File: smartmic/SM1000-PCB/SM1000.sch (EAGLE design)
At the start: 140 parts, among them CN1 HDR100-6, CN2 MOLEX-MINI-B-SMT, CN3 RASM712PX, CN4 RJ-45, CN5 MJ-3523-SMT, CN6 MJ-3523-SMT, CN7 MJ-3523-SMT, CN8 MJ-3523-SMT, CN9 MJ-3523-SMT, IC1 DIL-16, J1 JMP-2PIN, J2 JMP-2PIN, J3 JMP-2PIN, J4 JMP-2PIN, J5 JMP-2PIN, Q1 MMBT4401, Q2 MMBT4401, SW1 SW-SPST-2-1437565-0, SW2 SW-SPST-2-1437565-0, SW3 DPDT, T1 LM-NP-1001-B1L, T2 LM-NP-1001-B1L, U1 STM32F407, U2 LD3985M33R, U3 STMPS2141, U4 EMIF02-USB03F2, U5 TPS54329E, U6 LMV341, U7 LMV341, U8 LM386M-1, X1 8.0MHz

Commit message: Update Revision Header on Schematic
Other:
- note added: "04/21/14"
- note added: "Added to SourceForge Repository"
- note added: "RGB"
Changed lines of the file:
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@@
 <text x="347.472" y="17.272" size="3.81" layer="94" ratio="10">SmartMic Circuit Board</text>
 <text x="420.624" y="6.35" size="3.81" layer="94" ratio="10">.2</text>
+<text x="358.14" y="274.32" size="1.4224" layer="94" ratio="10">04/21/14</text>
+<text x="370.84" y="274.32" size="1.4224" layer="94" ratio="10">Added to SourceForge Repository</text>
+<text x="426.72" y="274.32" size="1.4224" layer="94" ratio="10">RGB</text>
 </plain>
 <instances>

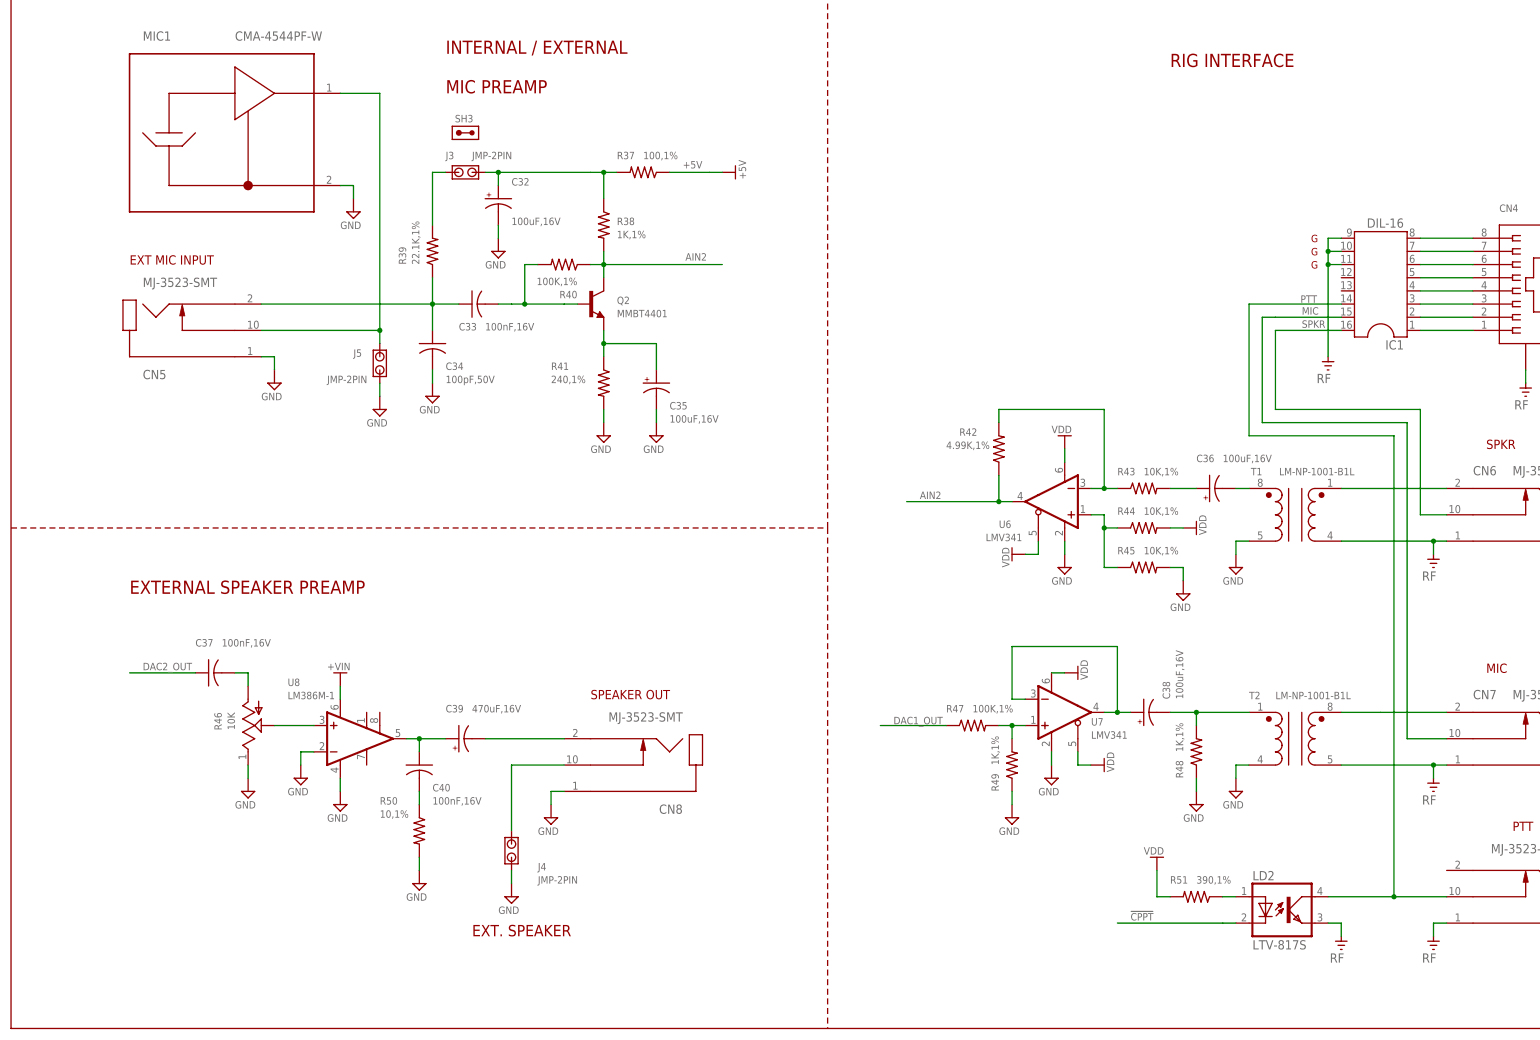
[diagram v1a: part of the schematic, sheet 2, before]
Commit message: 
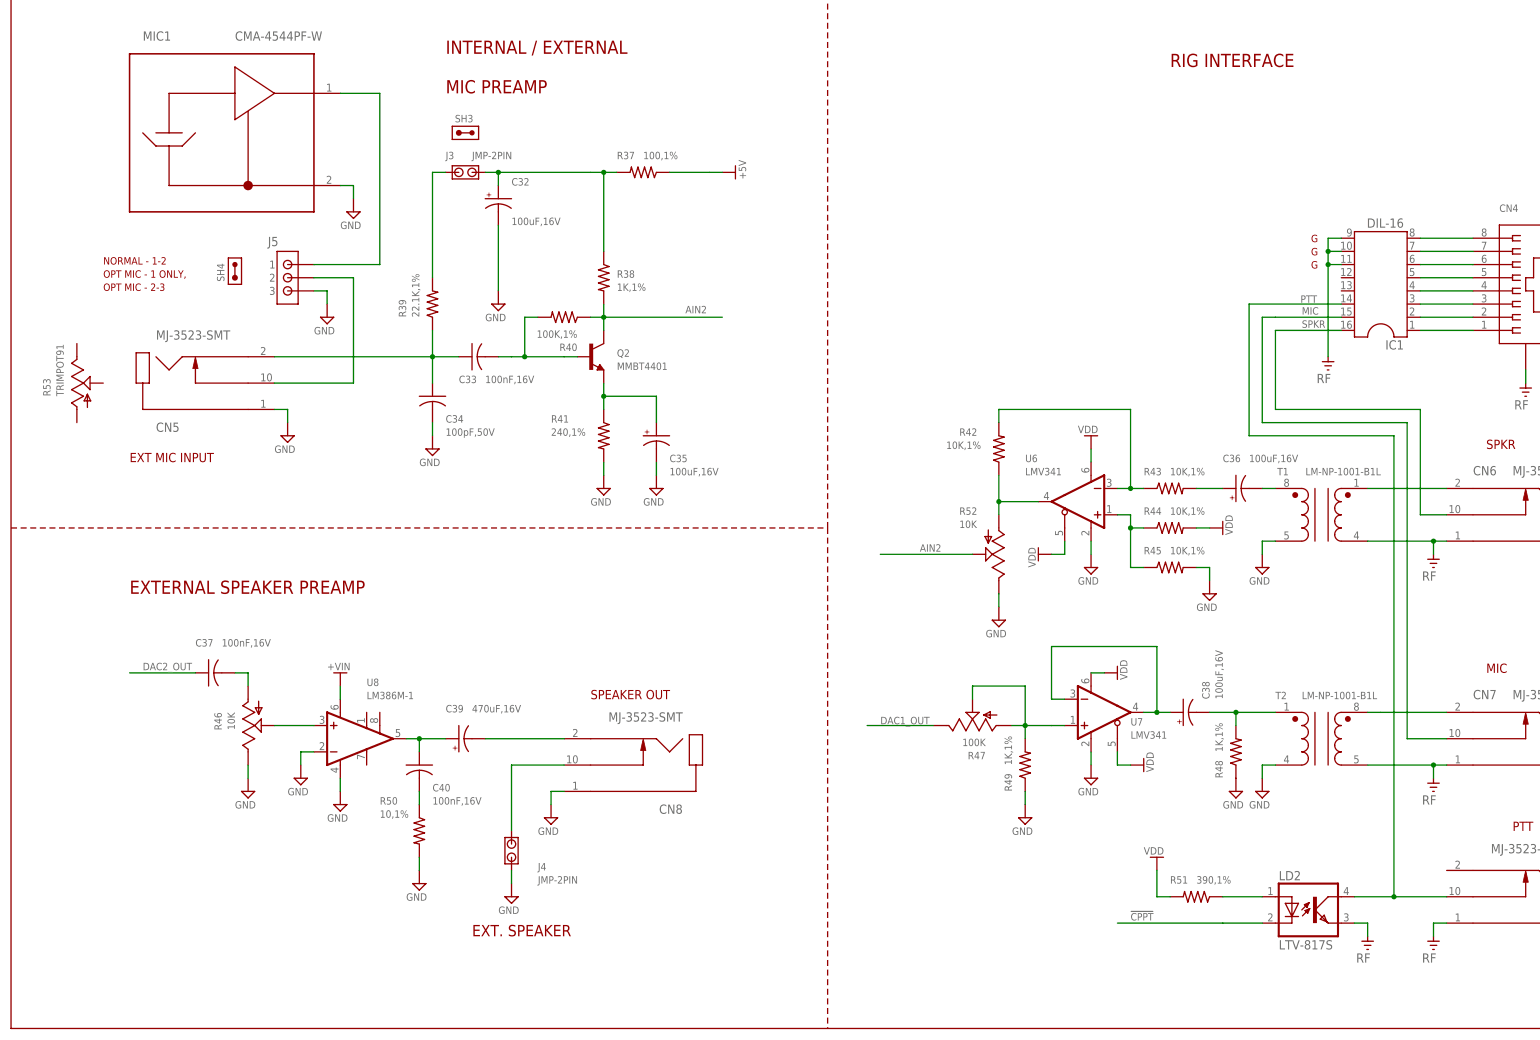
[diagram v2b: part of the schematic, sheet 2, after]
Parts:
- added R52: 10K, _RoweTel:TRIMPOT91
- added R53: TRIMPOT91, _RoweTel:TRIMPOT91
- added SH4: SHUNT,0.1IN, _Coherix:SHUNT,0.1IN
- J5: value JMP-2PIN -> JMPR-3PIN; device _Coherix:JMP-2PIN -> _Coherix:JMPR-3PIN
- LED1: value LED-GRN -> LED-RED
- LED2: value LED-ORG -> LED-RED
- LED3: value LED-RED -> LED-GRN
- LED4: value LED-BLU -> LED-YEL
- R42: value 4.99K,1% -> 10K,1%
- R47: value 100K,1% -> 100K; device _RoweTel:RES0603 -> _RoweTel:TRIMPOT91
- U8: device AA-IC:LM386M-1 -> _RoweTel:LM386M-1
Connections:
- net LED-BLU renamed LED-ERR
- net LED-GRN renamed LED-PWR
- net LED-ORG renamed LED-PTT
- net LED-RED renamed LED-RT
- new net N$48: R42.1, R52.3, U6.OUT
- new net N$60: CN5.10, J5.2
- net AIN2: now also R52.2; no longer R42.1, U6.OUT
- net GND: now also J5.3, R52.1; no longer J5.2
- net N$32: no longer CN5.10
- net N$90: now also R47.3
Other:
- note added: "CHANGE LED VALUES IN BOM DB"
- note added: "NORMAL - 1-2"
- note added: "OPT MIC - 1 ONLY,"
- note added: "OPT MIC - 2-3"
- moved on the sheet: C33, C34, C35, C36, C38, CN5, LD2, Q2, R38, R39, R40, R41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

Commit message: SM1000
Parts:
- removed J4: JMP-2PIN, _Coherix:JMP-2PIN
- added C41, C42, C43, C45: 100nF,16V, _RoweTel:CAP-0603
- added C44: 100nf,16V, _RoweTel:CAP-0603
- added FB1, FB2, FB3, FB4, FB6: FB0805, _RoweTel:FB0805
- added FB5: FB1210, _RoweTel:FB1210
- added R54: 1K,1%, _RoweTel:RES0603
- C22, C23: device _Coherix:CAP-0603 -> _RoweTel:CAP-0603
- LED1, LED2, LED3, LED4: device _Coherix:LED-SML-LX0603IW-TR -> _RoweTel:LTST-S220K
- R53: value TRIMPOT91 -> 10K
- T1, T2: value LM-NP-1001-B1L -> SM-LP-5001; device _RoweTel:LM-NP-1001-B1L -> _RoweTel:SM-LP-5001
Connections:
- removed net N$37: C25.1, R33.1, R34.1, SW3.6, U5.VIN
- new net N$70: Q2.C, R38.2, R40.1, R53.1
- new net N$72: CN7.2, FB2.2
- new net N$73: CN9.2, FB6.2
- new net N$74: FB6.1, LD2.COL
- new net N$75: CN8.2, FB3.2
- new net N$76: CN5.2, FB4.1
- new net N$77: CN3.2, FB5.1
- new net N$78: FB5.2, SW3.5
- net +3.3V: no longer LD1.4
- net +5V: now also C22.1
- net +VIN: now also C23.1, C25.1, R33.1, R34.1, SW3.6, U5.VIN; no longer CN3.2, SW3.5
- net AIN2: now also R53.2; no longer Q2.C, R38.2, R40.1
- net GND: now also C41.2, C42.2, R53.3, R54.1, T1.3, T2.3; no longer J4.1, T1.5, T2.4
- net MIC: now also C44.1
- net N$25: now also FB4.2; no longer CN5.2
- net N$33: now also FB1.1, T1.6; no longer CN6.2, T1.1
- net N$44: now also FB3.1; no longer CN8.2
- net N$61: now also FB2.1, T2.6; no longer CN7.2, T2.8
- net N$63: now also R54.2, T1.1; no longer T1.8
- net N$64: now also CN6.2, FB1.2; no longer CN8.10, J4.2
- net PTT: now also C45.1; no longer LD2.COL
- net RF: now also C43.2, C44.2, C45.2, T2.4; no longer T2.5
- net SPKR: now also C43.1
- net VDD: now also C41.1, C42.1, LD1.4; no longer C22.1, C23.1
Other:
- note added: "Add RC & L filtering to I/O & PS"
- moved on the sheet: C32, C33, C34, C35, C36, C38, CN4, CN5, CN6, CN7, CN8, CN9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

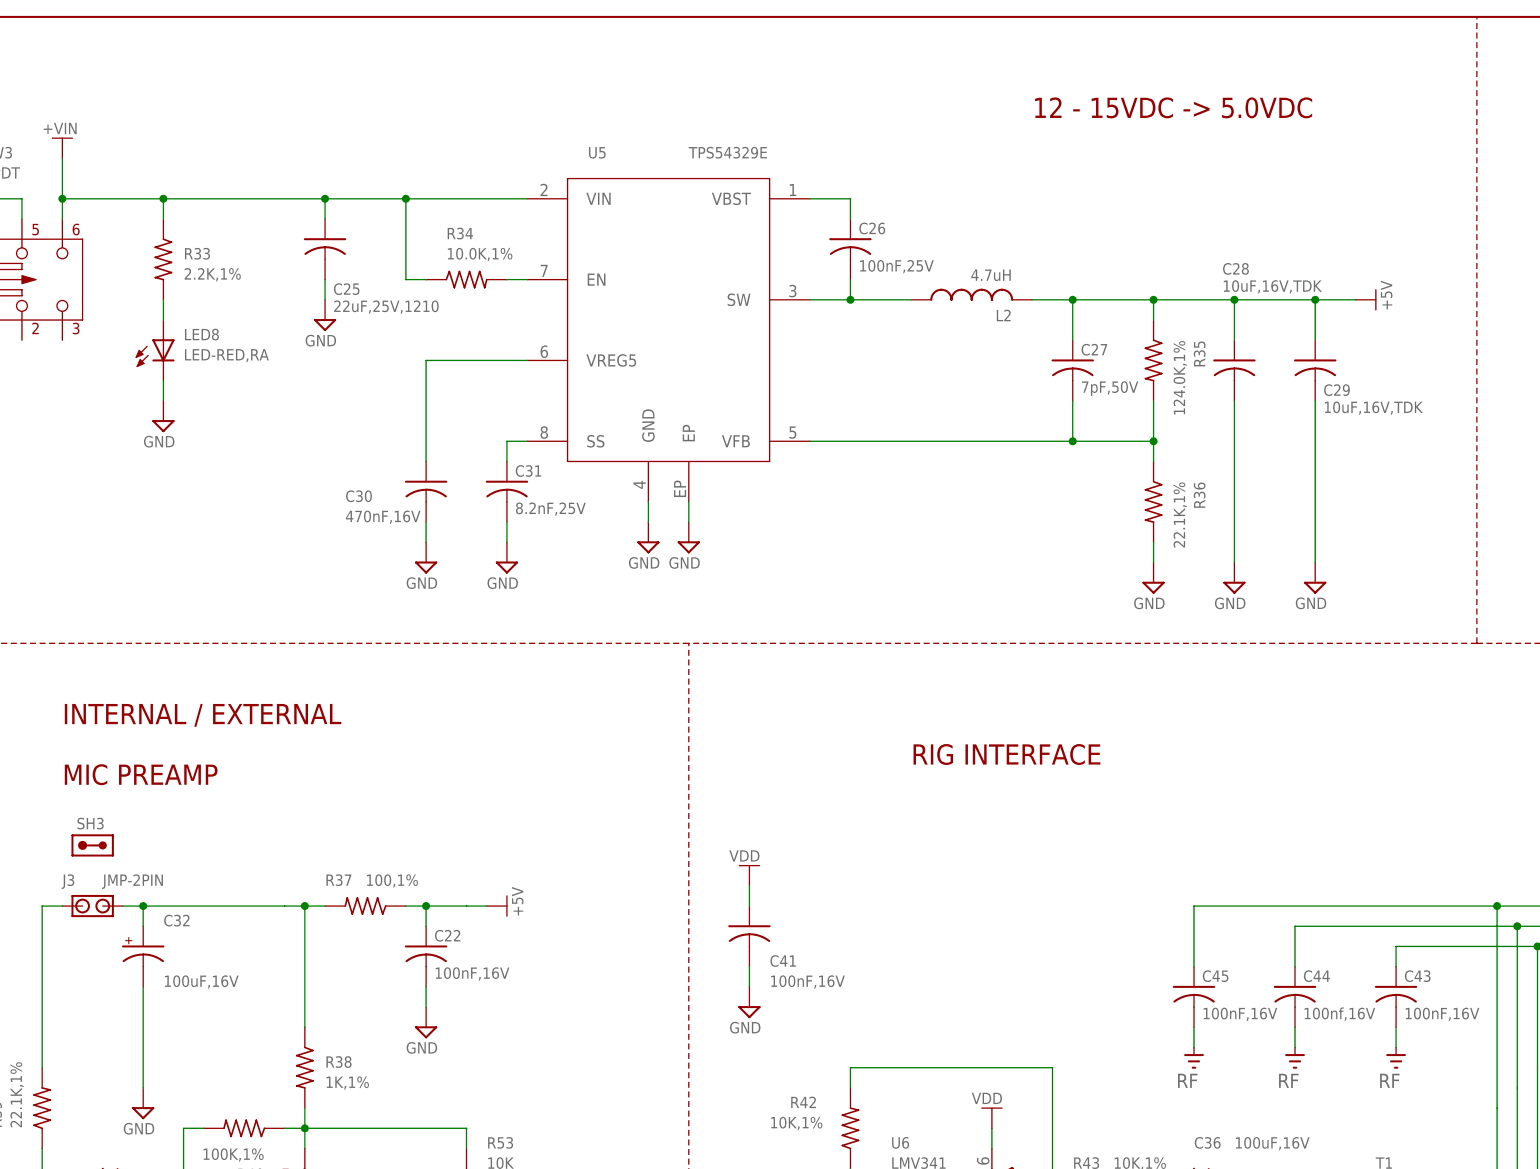
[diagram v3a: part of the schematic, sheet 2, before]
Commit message: 
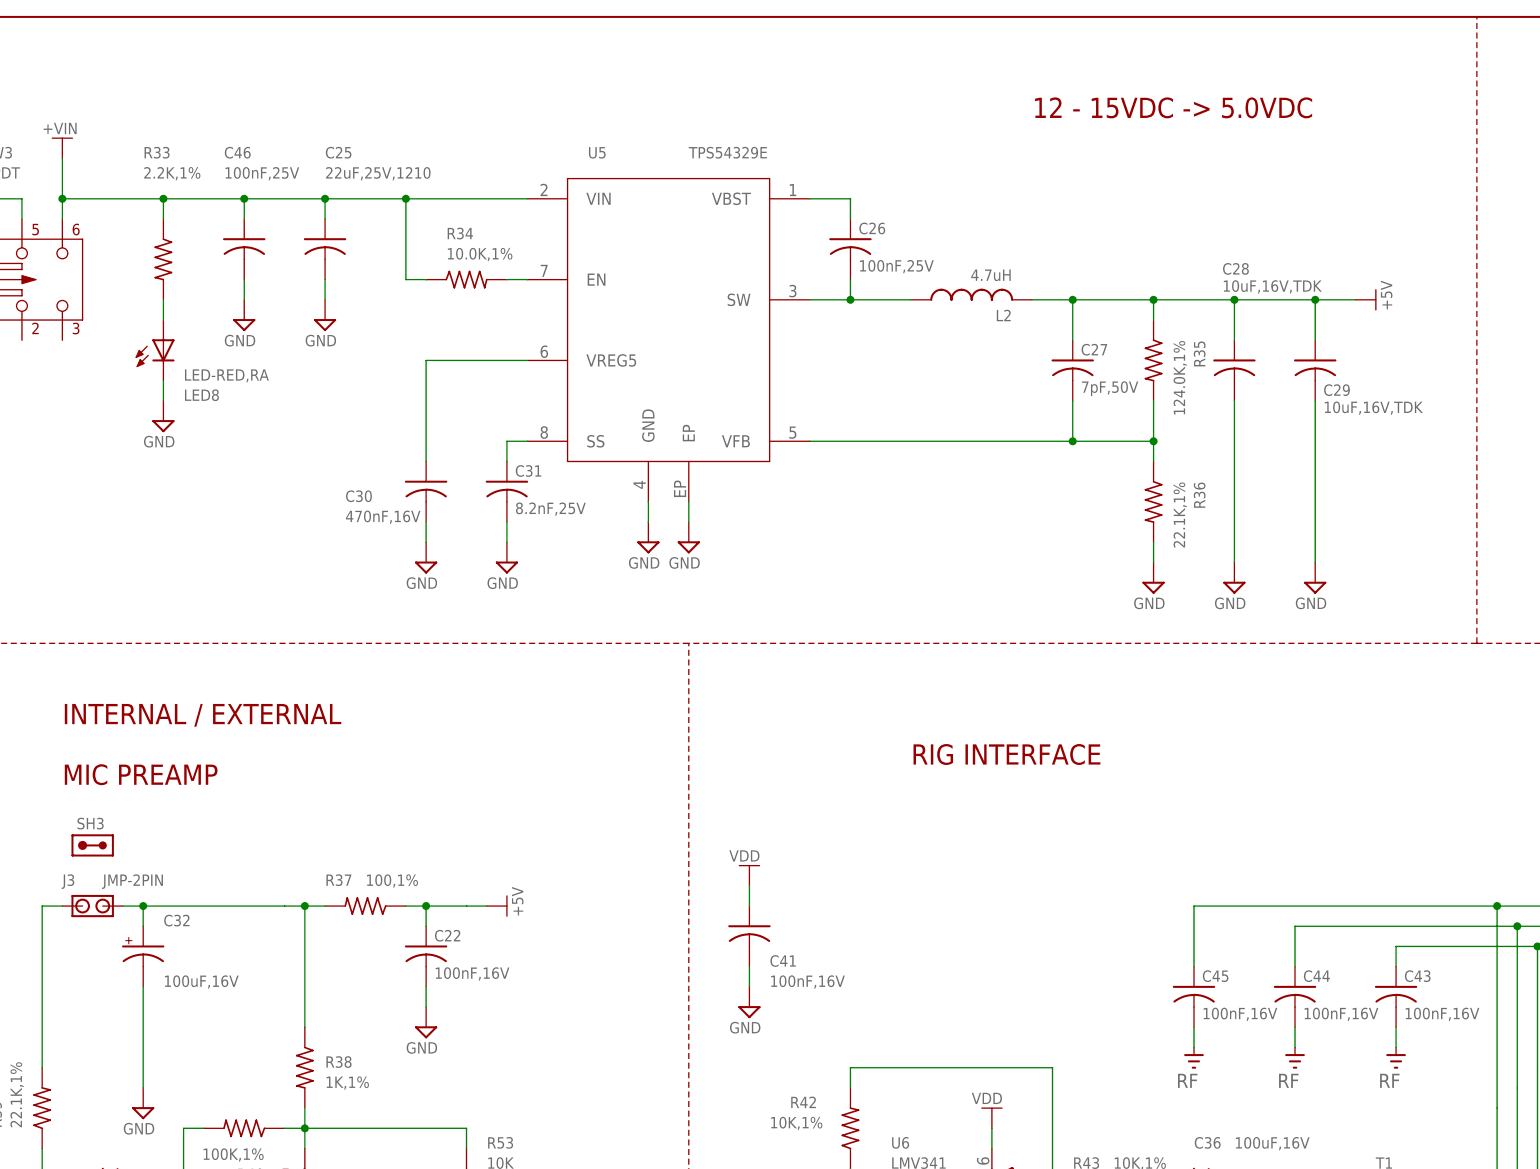
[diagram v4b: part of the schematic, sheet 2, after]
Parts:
- added C46: 100nF,25V, _RoweTel:CAP-0603
- C44: value 100nf,16V -> 100nF,16V
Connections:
- net +VIN: now also C46.1
- net GND: now also C46.2
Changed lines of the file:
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@@
 <part name="FB6" library="_RoweTel" deviceset="FB0805" device=""/>
 <part name="C43" library="_RoweTel" deviceset="CAP-0603" device="" value="100nF,16V"/>
-<part name="C44" library="_RoweTel" deviceset="CAP-0603" device="" value="100nf,16V"/>
+<part name="C44" library="_RoweTel" deviceset="CAP-0603" device="" value="100nF,16V"/>
 <part name="C45" library="_RoweTel" deviceset="CAP-0603" device="" value="100nF,16V"/>
 <part name="V97" library="A-SUPPLY2" deviceset="RF" device=""/>
@@
 <part name="V100" library="A-SUPPLY2" deviceset="GND" device=""/>
 <part name="V101" library="A-SUPPLY2" deviceset="VDD" device=""/>
+<part name="C46" library="_RoweTel" deviceset="CAP-0603" device="" value="100nF,25V"/>
+<part name="V102" library="A-SUPPLY2" deviceset="GND" device=""/>
 </parts>
 <sheets>
@@
 </instance>
 <instance part="C25" gate="G$1" x="111.76" y="251.46" smashed="yes">
-<attribute name="NAME" x="112.776" y="244.475" size="1.4224" layer="95" ratio="9"/>
-<attribute name="VALUE" x="112.776" y="242.316" size="1.4224" layer="96" ratio="9"/>
+<attribute name="NAME" x="111.76" y="261.62" size="1.4224" layer="95" ratio="9"/>
+<attribute name="VALUE" x="111.76" y="259.08" size="1.4224" layer="96" ratio="9"/>
 </instance>
 <instance part="V52" gate="GND" x="111.76" y="241.3"/>
@@
 <instance part="SH3" gate="G$1" x="81.28" y="175.26"/>
 <instance part="R33" gate="G$1" x="91.44" y="248.92" smashed="yes" rot="R270">
-<attribute name="NAME" x="93.98" y="248.92" size="1.4224" layer="95" ratio="9"/>
-<attribute name="VALUE" x="93.98" y="246.38" size="1.4224" layer="96" ratio="9"/>
+<attribute name="NAME" x="88.9" y="261.62" size="1.4224" layer="95" ratio="9"/>
+<attribute name="VALUE" x="88.9" y="259.08" size="1.4224" layer="96" ratio="9"/>
 </instance>
 <instance part="LED8" gate="G$1" x="91.44" y="238.76" smashed="yes">
-<attribute name="NAME" x="93.98" y="238.76" size="1.4224" layer="95" ratio="9"/>
-<attribute name="VALUE" x="93.98" y="236.22" size="1.4224" layer="96" ratio="9"/>
+<attribute name="NAME" x="93.98" y="231.14" size="1.4224" layer="95" ratio="9"/>
+<attribute name="VALUE" x="93.98" y="233.68" size="1.4224" layer="96" ratio="9"/>
 </instance>
 <instance part="V58" gate="GND" x="91.44" y="228.6"/>
@@
 </instance>
 <instance part="V100" gate="GND" x="228.6" y="114.3"/>
+<instance part="C46" gate="G$1" x="101.6" y="251.46" smashed="yes">
+<attribute name="NAME" x="99.06" y="261.62" size="1.4224" layer="95" ratio="9"/>
+<attribute name="VALUE" x="99.06" y="259.08" size="1.4224" layer="96" ratio="9"/>
+</instance>
+<instance part="V102" gate="GND" x="101.6" y="241.3"/>
 </instances>
 <busses>
@@
 <wire x1="228.6" y1="119.38" x2="228.6" y2="116.84" width="0.1524" layer="91"/>
 <pinref part="V100" gate="GND" pin="GND"/>
+</segment>
+<segment>
+<pinref part="C46" gate="G$1" pin="2"/>
+<wire x1="101.6" y1="246.38" x2="101.6" y2="243.84" width="0.1524" layer="91"/>
+<pinref part="V102" gate="GND" pin="GND"/>
 </segment>
 </net>
@@
 <junction x="111.76" y="256.54"/>
 <pinref part="SW3" gate="G$1" pin="6"/>
-<wire x1="91.44" y1="256.54" x2="111.76" y2="256.54" width="0.1524" layer="91"/>
+<wire x1="91.44" y1="256.54" x2="101.6" y2="256.54" width="0.1524" layer="91"/>
+<wire x1="101.6" y1="256.54" x2="111.76" y2="256.54" width="0.1524" layer="91"/>
 <wire x1="91.44" y1="256.54" x2="91.44" y2="254" width="0.1524" layer="91"/>
 <pinref part="R33" gate="G$1" pin="1"/>
@@
 <wire x1="78.74" y1="256.54" x2="78.74" y2="261.62" width="0.1524" layer="91"/>
 <junction x="78.74" y="256.54"/>
-</segment>
-<segment>
+<pinref part="C46" gate="G$1" pin="1"/>
+<wire x1="101.6" y1="254" x2="101.6" y2="256.54" width="0.1524" layer="91"/>
+<junction x="101.6" y="256.54"/>
+</segment>
+<segment>

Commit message: 
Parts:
- removed R11: 220K,1%, _Coherix:RES0603
- removed SW1: SW-SPST-2-1437565-0, _RoweTel:SW-SPST-2-1437565-0
- LED1, LED2: value LED-RED -> LED-RED,RA
- LED3: value LED-GRN -> LED-GRN,RA
- LED4: value LED-YEL -> LED-YEL,RA
- LED5: value LED-RED -> LED-RED,V
- LED6, LED7: value LED-GRN -> LED-GRN,V
- LED8: device _Coherix:LED-SML-LX0603IW-TR -> _RoweTel:LTST-S220K
- R10: value 330,1% -> 47,1%
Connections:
- removed net WAKE_UP: R10.1, U1A.PA0
- net GND: no longer R11.1
- net N$4: now also C10.1, C11.1, U1B.VREF+; no longer R11.2, SW1.P$1, SW1.P$2
- net N$5: now also R10.1; no longer C10.1, C11.1, U1B.VREF+
- net STLINK: now also U1A.PA0
- net VDD: no longer SW1.P$3, SW1.P$4
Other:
- note added: "04/25/14"
- note added: "A"
- note added: "Pre-Release to Prototype"
- note removed: ".2"
- note removed: "WAKE UP SW"
- moved on the sheet: C1, C10, C11, C12, C13, C16, C17, C18, C19, C20, C21, L1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
